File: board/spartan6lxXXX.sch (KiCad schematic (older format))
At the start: 118 parts, among them U12 SPARTAN6LXXXX-CSG324, U13 FXO-HC536R, U2 M25P16

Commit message: Issue #1027 - Schematics final changes.
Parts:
- removed R114: 4.7K, ~, symbol R
- added R367, R368, R369: 10K, ~, symbol R
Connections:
- wire segments 403 -> 409
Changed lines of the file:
@@
 Sheet 5 8
 Title "HDMI2USB"
-Date "9 apr 2014"
+Date "11 apr 2014"
 Rev ""
 Comp ""
@@
 DONE
 $Comp
-L R R114
-U 1 1 530D0387
-P 14800 9700
-F 0 "R114" V 14900 9700 40  0000 C CNN
-F 1 "4.7K" V 14807 9701 40  0000 C CNN
-F 2 "~" V 14730 9700 30  0000 C CNN
-F 3 "~" H 14800 9700 30  0000 C CNN
-	1    14800 9700
-	-1   0    0    1
-$EndComp
-$Comp
 L R R116
 U 1 1 530D039C
@@
 	0    1    1    0
 $EndComp
-Text Label 14400 9950 0    39   ~ 0
-PROG_B
 Text Label 14400 10100 0    39   ~ 0
 DONE
@@
 	0    -1   -1   0
 $EndComp
+$Comp
+L R R331
+U 1 1 53567479
+P 1850 8950
+F 0 "R331" V 1900 8700 40  0000 C CNN
+F 1 "0R" V 1857 8951 40  0000 C CNN
+F 2 "~" V 1780 8950 30  0000 C CNN
+F 3 "~" H 1850 8950 30  0000 C CNN
+	1    1850 8950
+	0    -1   -1   0
+$EndComp
+$Comp
+L R R332
+U 1 1 53567C15
+P 1850 9300
+F 0 "R332" V 1900 9600 40  0000 C CNN
+F 1 "0R" V 1857 9301 40  0000 C CNN
+F 2 "~" V 1780 9300 30  0000 C CNN
+F 3 "~" H 1850 9300 30  0000 C CNN
+	1    1850 9300
+	0    -1   -1   0
+$EndComp
+$Comp
+L R R330
+U 1 1 5356911B
+P 1850 8500
+F 0 "R330" V 1900 8750 40  0000 C CNN
+F 1 "0R" V 1857 8501 40  0000 C CNN
+F 2 "~" V 1780 8500 30  0000 C CNN
+F 3 "~" H 1850 8500 30  0000 C CNN
+	1    1850 8500
+	0    -1   -1   0
+$EndComp
+Text Notes 550  700  0    59   ~ 0
+SPARTAN6 XC6SLXXXX
+Text HLabel 11650 7250 0    60   Output ~ 0
+DDR-A[0..12]
+$Comp
+L R R367
+U 1 1 5353E60C
+P 11200 10100
+F 0 "R367" V 11100 10100 40  0000 C CNN
+F 1 "10K" V 11207 10101 40  0000 C CNN
+F 2 "~" V 11130 10100 30  0000 C CNN
+F 3 "~" H 11200 10100 30  0000 C CNN
+	1    11200 10100
+	0    -1   -1   0
+$EndComp
+$Comp
+L R R368
+U 1 1 5353E896
+P 13350 10400
+F 0 "R368" V 13250 10400 40  0000 C CNN
+F 1 "10K" V 13357 10401 40  0000 C CNN
+F 2 "~" V 13280 10400 30  0000 C CNN
+F 3 "~" H 13350 10400 30  0000 C CNN
+	1    13350 10400
+	0    -1   -1   0
+$EndComp
 Wire Wire Line
 	10900 1350 11450 1350
@@
 Connection ~ 15300 9150
 Wire Wire Line
-	14800 9450 14800 9150
-Connection ~ 14800 9150
-Wire Wire Line
-	14800 9950 14400 9950
-Wire Wire Line
 	15300 9900 15300 10100
 Wire Wire Line
@@
 Connection ~ 11650 9200
 Connection ~ 11550 9200
-Wire Bus Line
-	14200 10450 10200 10450
-Wire Bus Line
-	14200 9100 14200 10450
-Wire Bus Line
-	10200 10450 10200 9100
-Wire Bus Line
-	10200 9100 14200 9100
-Wire Bus Line
-	12200 7750 12200 9050
-Wire Bus Line
-	12200 9050 14050 9050
-Wire Bus Line
-	14050 9050 14050 7750
-Wire Bus Line
-	14050 7750 12200 7750
 Wire Wire Line
 	10600 8550 10300 8550
@@
 Wire Wire Line
 	14850 8950 14500 8950
-Wire Bus Line
-	14350 8100 14350 10550
-Wire Bus Line
-	14350 10550 15900 10550
-Wire Bus Line
-	15900 10550 15900 8100
-Wire Bus Line
-	15900 8100 14350 8100
-Wire Bus Line
-	12200 8850 13150 8850
-Wire Bus Line
-	13150 8850 13150 9050
-Wire Bus Line
-	11150 9100 11150 9250
-Wire Bus Line
-	11150 9250 10200 9250
-Wire Bus Line
-	14350 8250 15400 8250
-Wire Bus Line
-	15400 8250 15400 8100
-Wire Bus Line
-	10150 8600 10150 11200
-Wire Bus Line
-	10150 11200 2700 11200
-Wire Bus Line
-	2700 11200 2700 8450
-Wire Bus Line
-	2700 8450 10150 8450
-Wire Bus Line
-	10150 8450 10150 8650
-Wire Bus Line
-	2700 8600 3900 8600
-Wire Bus Line
-	3900 8600 3900 8450
-Wire Bus Line
-	500  7900 500  11200
-Wire Bus Line
-	500  11200 2550 11200
-Wire Bus Line
-	2550 11200 2550 8400
-Wire Bus Line
-	2550 8400 4600 8400
-Wire Bus Line
-	4600 8400 4600 7700
-Wire Bus Line
-	4600 7700 500  7700
-Wire Bus Line
-	500  7700 500  7950
-Wire Bus Line
-	500  7850 1600 7850
-Wire Bus Line
-	1600 7850 1600 7700
 Wire Wire Line
 	1500 9600 1500 9800
@@
 Wire Wire Line
 	2150 11100 2100 11100
-$Comp
-L R R331
-U 1 1 53567479
-P 1850 8950
-F 0 "R331" V 1900 8700 40  0000 C CNN
-F 1 "0R" V 1857 8951 40  0000 C CNN
-F 2 "~" V 1780 8950 30  0000 C CNN
-F 3 "~" H 1850 8950 30  0000 C CNN
-	1    1850 8950
-	0    -1   -1   0
-$EndComp
 Wire Wire Line
 	1500 8800 1500 8950
@@
 Wire Wire Line
 	2300 9050 2250 9050
-$Comp
-L R R332
-U 1 1 53567C15
-P 1850 9300
-F 0 "R332" V 1900 9600 40  0000 C CNN
-F 1 "0R" V 1857 9301 40  0000 C CNN
-F 2 "~" V 1780 9300 30  0000 C CNN
-F 3 "~" H 1850 9300 30  0000 C CNN
-	1    1850 9300
-	0    -1   -1   0
-$EndComp
 Wire Wire Line
 	1600 9300 1500 9300
@@
 Wire Wire Line
 	2250 9450 2100 9450
-$Comp
-L R R330
-U 1 1 5356911B
-P 1850 8500
-F 0 "R330" V 1900 8750 40  0000 C CNN
-F 1 "0R" V 1857 8501 40  0000 C CNN
-F 2 "~" V 1780 8500 30  0000 C CNN
-F 3 "~" H 1850 8500 30  0000 C CNN
-	1    1850 8500
-	0    -1   -1   0
-$EndComp
 Wire Wire Line
 	1600 8500 1500 8500
@@
 	2350 8650 2300 8650
 Wire Bus Line
-	500  550  500  7450
-Wire Bus Line
-	500  7450 16000 7450
-Wire Bus Line
-	16000 7450 16000 550
-Wire Bus Line
-	16000 550  500  550
-Text Notes 550  650  0    59   ~ 0
-SPARTAN6 XC6SLXXXX
-Wire Bus Line
-	500  650  500  700
-Wire Bus Line
-	500  700  1600 700
-Wire Bus Line
-	1600 700  1600 550
-Text HLabel 11650 7250 0    60   Output ~ 0
-DDR-A[0..12]
-Wire Bus Line
 	11650 7250 11900 7250
 Wire Bus Line
 	11900 7250 11900 4350
+Wire Notes Line
+	500  7700 4700 7700
+Wire Notes Line
+	4700 7700 4700 8400
+Wire Notes Line
+	4700 8400 2650 8400
+Wire Notes Line
+	2650 8400 2650 11150
+Wire Notes Line
+	2650 11150 500  11150
+Wire Notes Line
+	500  11150 500  7700
+Wire Notes Line
+	2750 8450 2750 11200
+Wire Notes Line
+	2750 11200 10100 11200
+Wire Notes Line
+	10100 11200 10100 8450
+Wire Notes Line
+	10100 8450 2750 8450
+Wire Notes Line
+	2750 8600 3900 8600
+Wire Notes Line
+	3900 8600 3900 8450
+Wire Notes Line
+	1600 7700 1600 7850
+Wire Notes Line
+	1600 7850 500  7850
+Wire Notes Line
+	10200 9100 14150 9100
+Wire Notes Line
+	14150 9100 14150 10550
+Wire Notes Line
+	14150 10550 10200 10550
+Wire Notes Line
+	10200 10550 10200 9100
+Wire Notes Line
+	13950 9000 13950 7750
+Wire Notes Line
+	13950 7750 12200 7750
+Wire Notes Line
+	12200 7750 12200 9000
+Wire Notes Line
+	13100 9000 13150 9000
+Wire Notes Line
+	12200 9000 13950 9000
+Wire Notes Line
+	13200 9000 13200 8900
+Wire Notes Line
+	13200 8900 12200 8900
+Wire Notes Line
+	14350 8050 15950 8050
+Wire Notes Line
+	15950 8050 15950 10550
+Wire Notes Line
+	15950 10550 14350 10550
+Wire Notes Line
+	14350 10550 14350 8050
+Wire Notes Line
+	15400 8050 15400 8250
+Wire Notes Line
+	15400 8250 14350 8250
+Wire Notes Line
+	500  7500 15950 7500
+Wire Notes Line
+	15950 7500 15950 600
+Wire Notes Line
+	15950 600  500  600
+Wire Notes Line
+	500  600  500  7500
+Wire Notes Line
+	500  700  1550 700
+Wire Notes Line
+	1550 700  1550 600
+Wire Wire Line
+	11500 9900 11500 10100
+Wire Wire Line
+	11500 10100 11450 10100
+Wire Wire Line
+	13100 10200 13100 10400
+Connection ~ 13100 10200
+$Comp
+L R R369
+U 1 1 5353F02F
+P 13550 9950
+F 0 "R369" V 13450 9950 40  0000 C CNN
+F 1 "10K" V 13557 9951 40  0000 C CNN
+F 2 "~" V 13480 9950 30  0000 C CNN
+F 3 "~" H 13550 9950 30  0000 C CNN
+	1    13550 9950
+	0    -1   -1   0
+$EndComp
+Wire Wire Line
+	13050 10050 13050 9950
+Wire Wire Line
+	13050 9950 13300 9950
+Wire Wire Line
+	13600 10400 13950 10400
+Wire Wire Line
+	13800 9950 14050 9950
+Text Label 14050 9950 2    39   ~ 0
+VCC3V3
+Wire Wire Line
+	10950 10100 10450 10100
+Text Label 10450 10100 0    39   ~ 0
+VCC3V3
+Text Label 13950 10400 2    39   ~ 0
+VCC3V3
 $EndSCHEMATC

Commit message: Issue #1027 - Schematics final changes.
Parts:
- added D5: LED, ~, symbol LED
- added R370: 1K, ~, symbol R
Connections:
- net labels added: CMPCS_B_2, LED-DEBUG, SPI-SCK
- net labels removed: SCK
- wire segments 409 -> 412
- no-connect marks 11 -> 10
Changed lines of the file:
@@
 Sheet 5 8
 Title "HDMI2USB"
-Date "11 apr 2014"
+Date "15 apr 2014"
 Rev ""
 Comp ""
@@
 VCC3V3
 Text HLabel 8200 1100 2    60   BiDi ~ 0
-SCK
+SPI-SCK
 Text HLabel 12750 6200 0    60   BiDi ~ 0
 PROG_B
@@
 NoConn ~ 10900 1250
 NoConn ~ 10900 1450
-NoConn ~ 10900 1550
 Text GLabel 15400 2150 2    60   Input ~ 0
 VCC3V3
@@
 SPI-SDI
 Text HLabel 13050 10050 2    60   BiDi ~ 0
-SCK
+SPI-SCK
 Text HLabel 13650 10200 2    60   BiDi ~ 0
 SPI-SDO
@@
 Text Label 13950 10400 2    39   ~ 0
 VCC3V3
+Wire Notes Line
+	10250 8400 10250 8950
+Wire Notes Line
+	10250 8400 11500 8400
+Wire Notes Line
+	11500 8400 11500 8950
+Wire Notes Line
+	11500 8950 10250 8950
+Text Label 12700 6000 0    39   ~ 0
+CMPCS_B_2
+Wire Wire Line
+	10900 1550 11200 1550
+Text Label 11200 1550 2    39   ~ 0
+LED-DEBUG
+Text Label 10000 8200 0    39   ~ 0
+LED-DEBUG
+$Comp
+L LED D5
+U 1 1 534D5C2A
+P 11050 8200
+F 0 "D5" H 11050 8300 50  0000 C CNN
+F 1 "LED" H 11050 8100 50  0000 C CNN
+F 2 "~" H 11050 8200 60  0000 C CNN
+F 3 "~" H 11050 8200 60  0000 C CNN
+	1    11050 8200
+	1    0    0    -1
+$EndComp
+$Comp
+L R R370
+U 1 1 534D5C40
+P 10600 8200
+F 0 "R370" V 10700 8200 40  0000 C CNN
+F 1 "1K" V 10607 8201 40  0000 C CNN
+F 2 "~" V 10530 8200 30  0000 C CNN
+F 3 "~" H 10600 8200 30  0000 C CNN
+	1    10600 8200
+	0    1    1    0
+$EndComp
+Wire Wire Line
+	10000 8200 10350 8200
+Text Label 11350 8200 2    39   ~ 0
+GND
+Wire Wire Line
+	11250 8200 11350 8200
 $EndSCHEMATC

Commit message: Issue #1027 - Schematics final changes.
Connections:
- net labels added: GNDT-NC1, GNDT-NC10, GNDT-NC11, GNDT-NC2, GNDT-NC3, GNDT-NC4, GNDT-NC5, GNDT-NC6, GNDT-NC7, GNDT-NC8, GNDT-NC9, NC-VCCAUXT1, NC-VCCAUXT2
- wire segments 412 -> 425
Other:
- note added: "SELECTION RESISTERS LX-LXT"
- moved on the sheet: D5, R160, R161, R162, R163, R164, R165, R166, R167, R168, R169, R170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

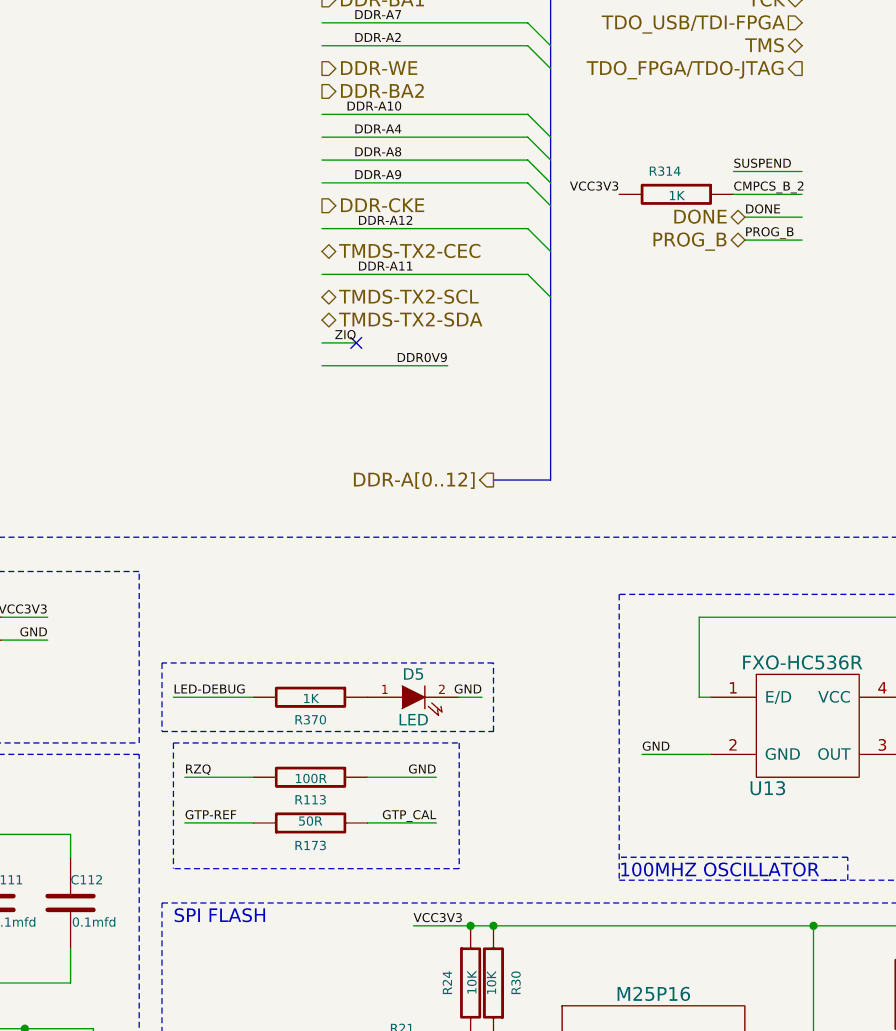
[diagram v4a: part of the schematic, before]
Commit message: Issue #1027 - Schematics final changes.
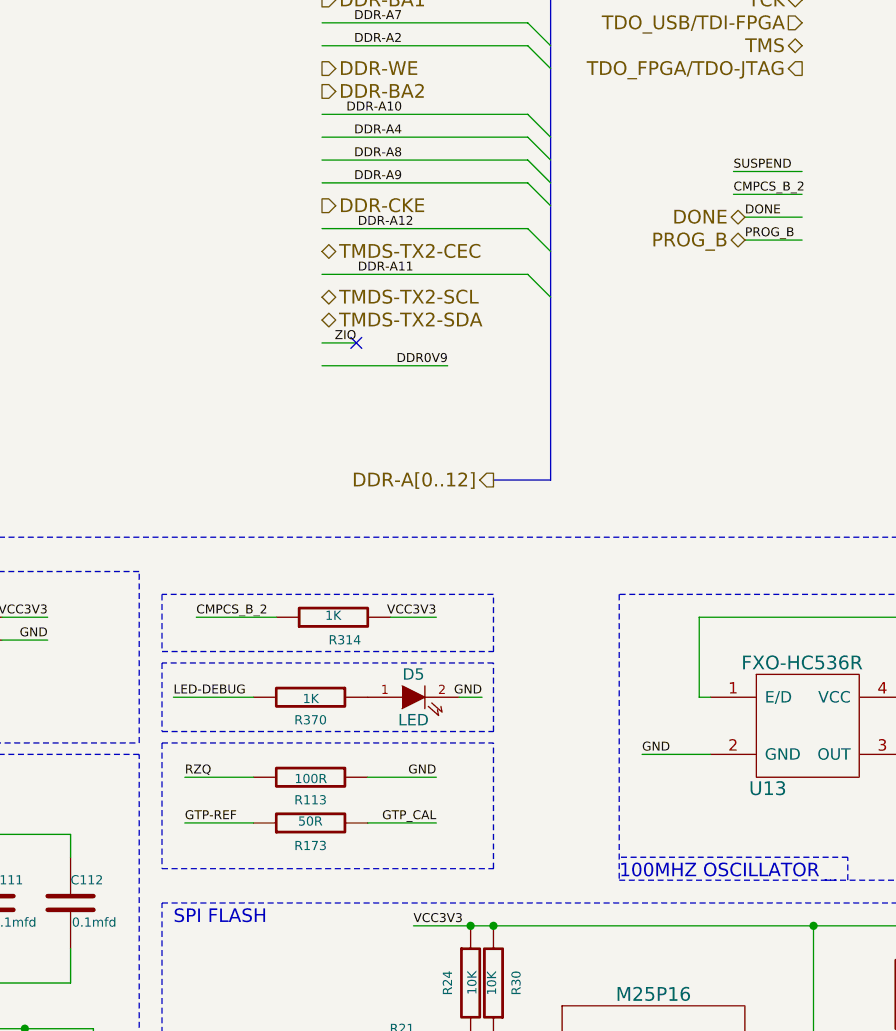
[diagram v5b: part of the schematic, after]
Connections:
- wire segments 425 -> 427
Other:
- moved on the sheet: R314
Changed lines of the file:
@@
 L R R314
 U 1 1 5329D6EA
-P 12450 6000
-F 0 "R314" V 12350 5950 40  0000 C CNN
-F 1 "1K" V 12457 6001 40  0000 C CNN
-F 2 "~" V 12380 6000 30  0000 C CNN
-F 3 "~" H 12450 6000 30  0000 C CNN
-	1    12450 6000
-	0    1    1    0
-$EndComp
-Text Label 12200 6000 2    39   ~ 0
+P 10950 7850
+F 0 "R314" V 10850 7800 40  0000 C CNN
+F 1 "1K" V 10957 7851 40  0000 C CNN
+F 2 "~" V 10880 7850 30  0000 C CNN
+F 3 "~" H 10950 7850 30  0000 C CNN
+	1    10950 7850
+	0    -1   -1   0
+$EndComp
+Text Label 11400 7850 2    39   ~ 0
 VCC3V3
 Text Label 15550 8850 2    39   ~ 0
@@
 VCC3V3
 Wire Notes Line
-	10250 8400 10250 8950
-Wire Notes Line
-	10250 8400 11500 8400
-Wire Notes Line
-	11500 8400 11500 8950
-Wire Notes Line
-	11500 8950 10250 8950
+	10200 8400 11650 8400
+Wire Notes Line
+	10200 8950 11650 8950
 Text Label 12700 6000 0    39   ~ 0
 CMPCS_B_2
@@
 Wire Notes Line
 	11650 8050 10200 8050
+Wire Wire Line
+	11200 7850 11400 7850
+Text Label 10350 7850 0    39   ~ 0
+CMPCS_B_2
+Wire Wire Line
+	10350 7850 10700 7850
+Wire Notes Line
+	10200 7750 10200 8000
+Wire Notes Line
+	10200 8000 11650 8000
+Wire Notes Line
+	11650 8000 11650 7750
+Wire Notes Line
+	11650 7750 10200 7750
+Wire Notes Line
+	11650 8950 11650 8400
+Wire Notes Line
+	10200 8400 10200 8950
 $EndSCHEMATC

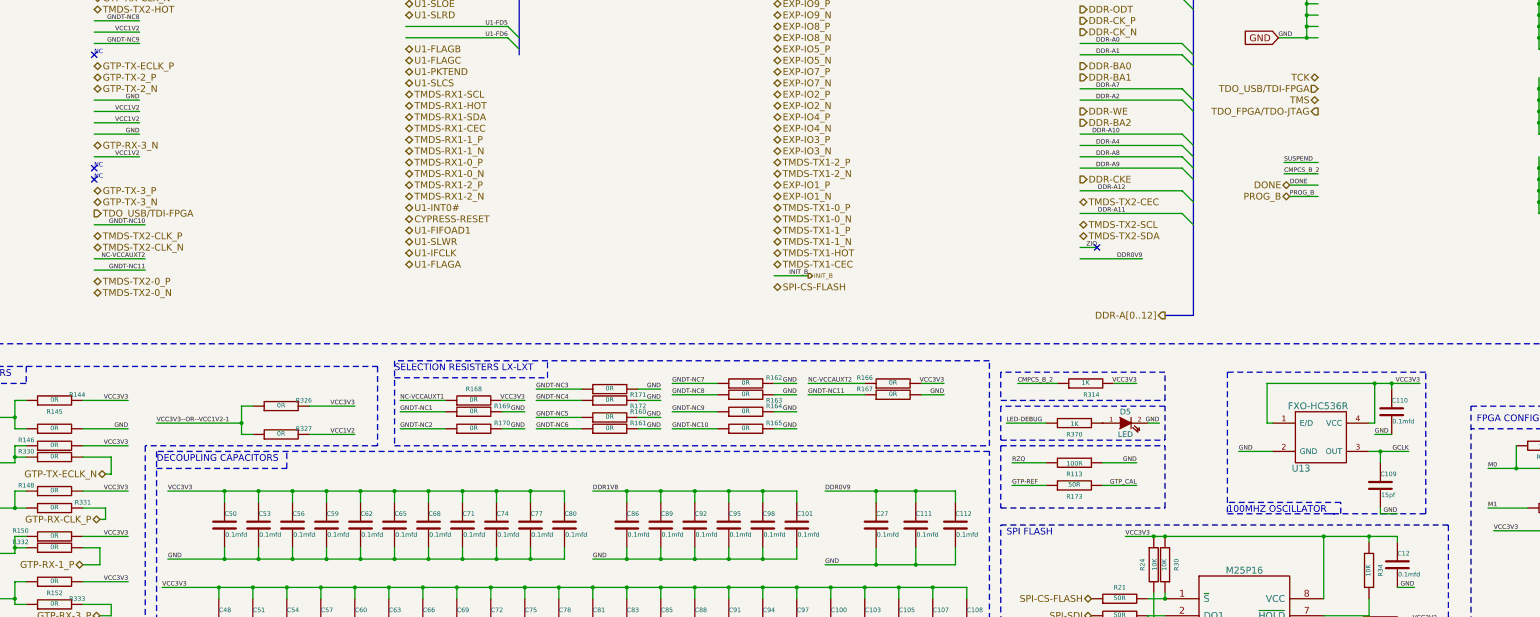
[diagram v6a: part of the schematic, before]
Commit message: Issue #1053 - Cypress routing
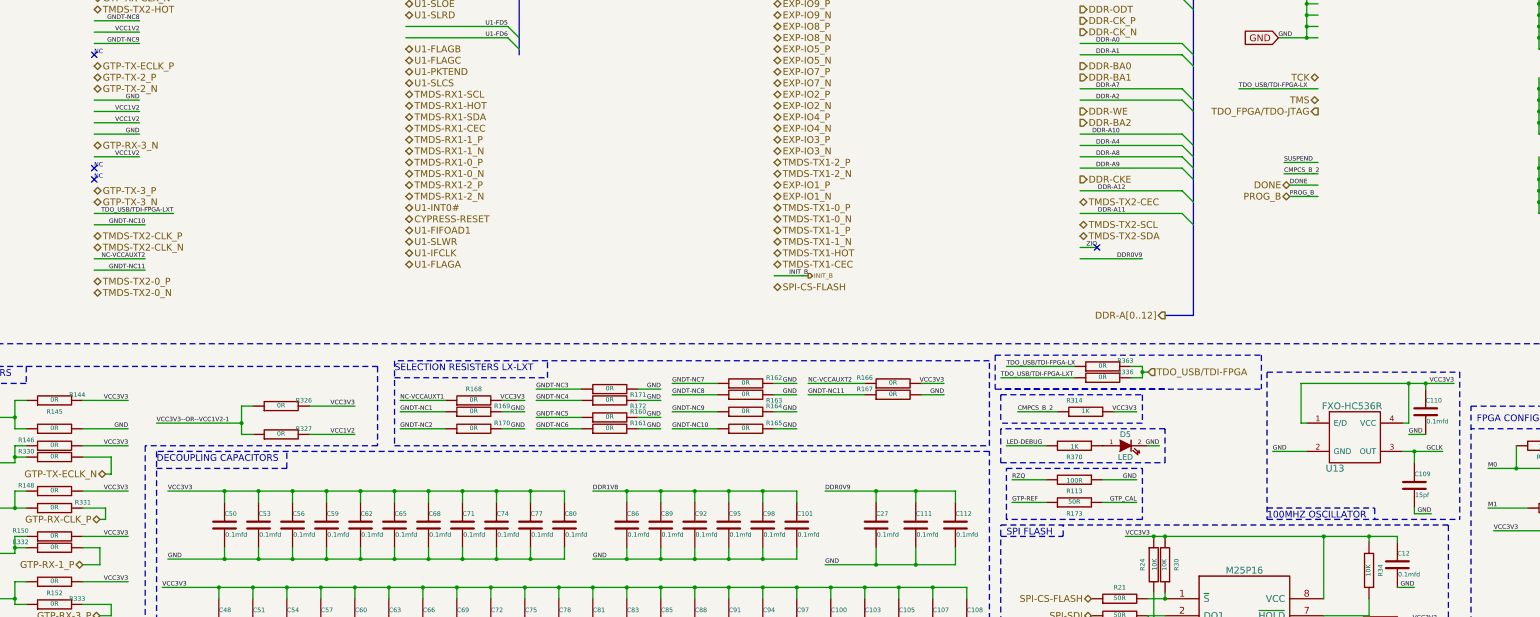
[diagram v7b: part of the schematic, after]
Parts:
- added R336, R363: 0R, ~, symbol R
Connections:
- net labels added: TDO_USB/TDI-FPGA-LX, TDO_USB/TDI-FPGA-LXT
- wire segments 427 -> 435
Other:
- moved on the sheet: C109, C110, D5, R113, R173, R314, R370, U13

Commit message: Issue #1053 - Cypress routing
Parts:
- added R364, R365, R366, R371, R372, R373: 0R, ~, symbol R
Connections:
- net labels added: GND--OR--VCC1V2-1, GND--OR--VCC1V2-2, VCC3V3--OR--GND1, VCC3V3--OR--GND2, VCC3V3--OR--GND3
- net labels removed: GND--OR--VCC1V2, VCC3V3--OR--GND
- wire segments 435 -> 455
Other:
- moved on the sheet: C100, C101, C102, C103, C104, C105, C106, C107, C108, C109, C110, C111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
